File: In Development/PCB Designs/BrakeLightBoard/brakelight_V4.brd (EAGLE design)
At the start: 68.6 x 38.1 mm, 21 parts, among them Q2 30N06L

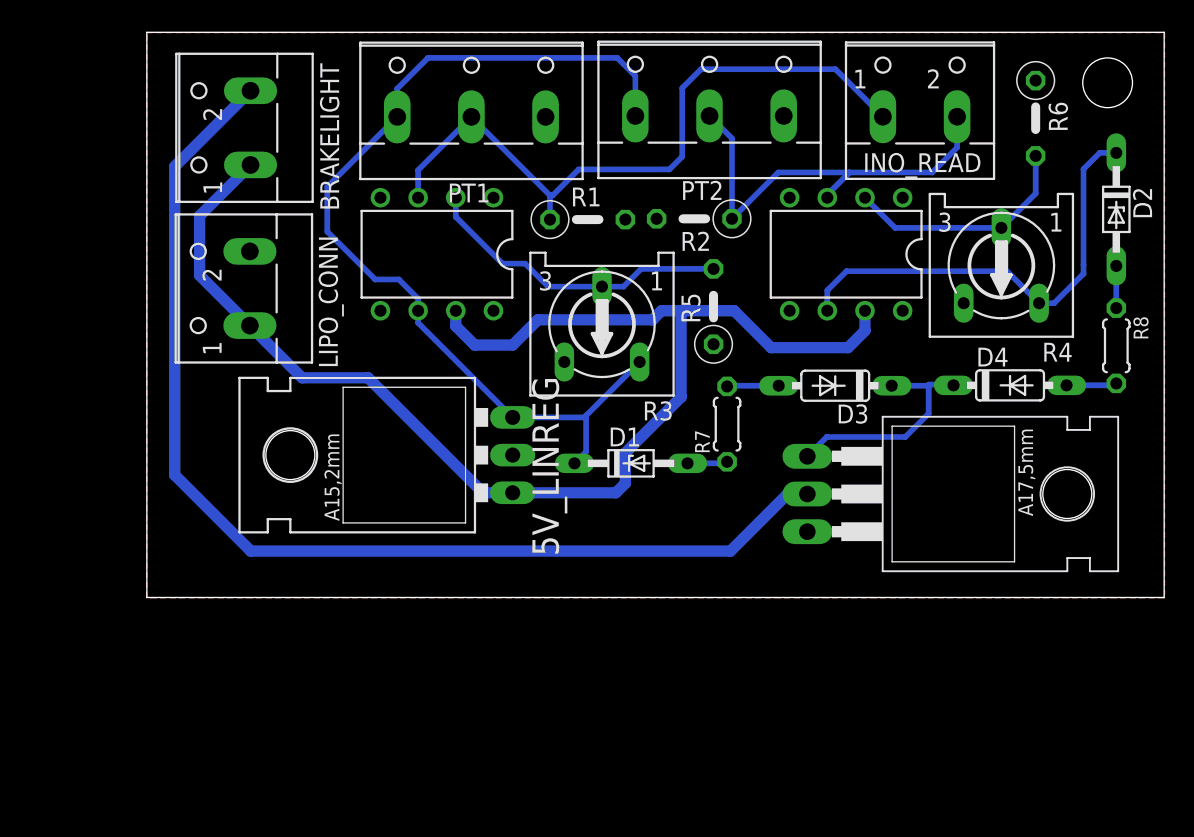
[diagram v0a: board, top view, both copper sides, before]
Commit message: Created new brakelight board using TLC2252
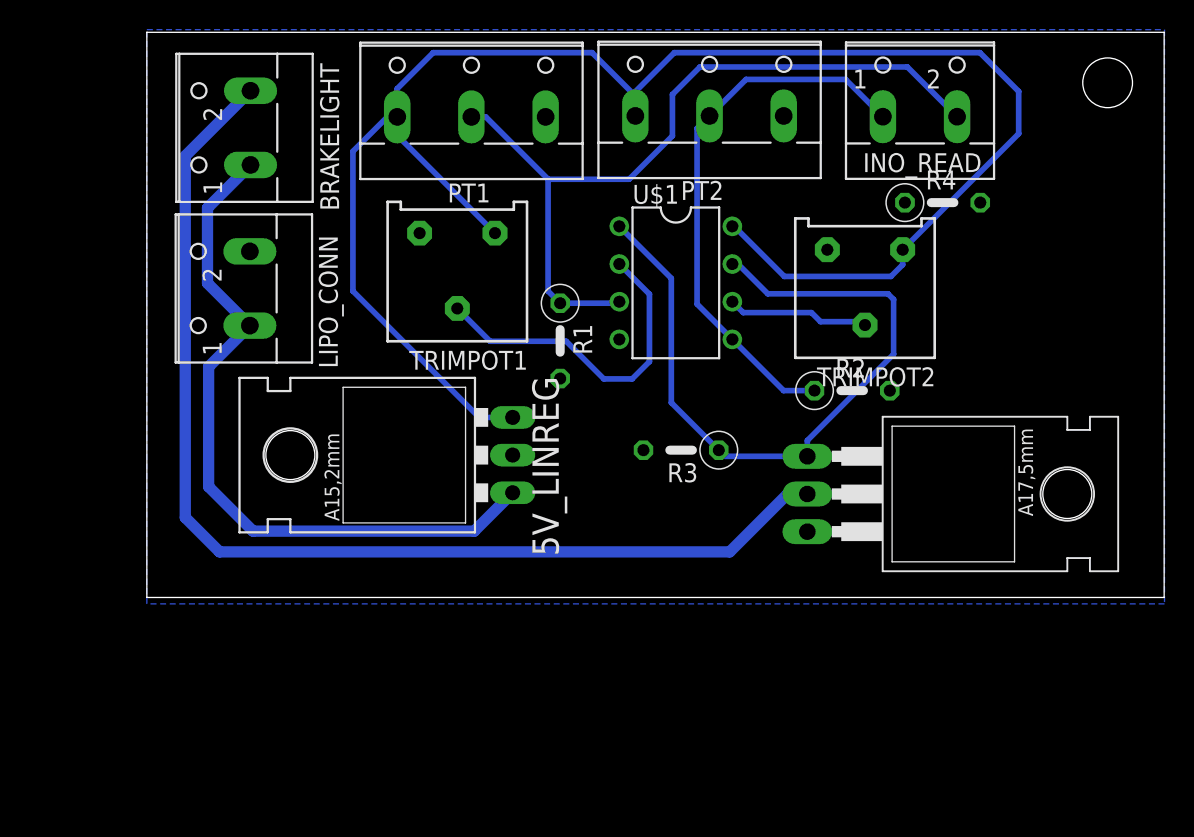
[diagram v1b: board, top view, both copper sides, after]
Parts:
- removed D1, D2: 1N5231, diode:DO34Z7
- removed D3, D4: 1N4148DO35-7, diode:DO35-7
- removed R5, R6: 560, 0ohmresistor:0207/5V
- removed R7, R8: (no value), 0ohmresistor:0204/5
- removed U$2: LM741, GTOR:DIL08
- added TRIMPOT1, TRIMPOT2: (no value), bourns:3386Y
- R1, R2: value 5.1k -> (none)
- R3, R4: value 10k -> (none); device pot:RS3 -> 0ohmresistor:0207/5V
- U$1: value LM741 -> TLC2252
- moved U$1 16.2 mm to (35.7, 21.2), turned to 270 degrees
- moved R2 15.7 mm to (47.5, 13.9), turned to 0 degrees
- moved R3 10.0 mm to (36.0, 9.93)
- moved R1 8.39 mm to (27.9, 17.3), turned to 270 degrees
- moved R4 5.80 mm to (53.6, 26.6), turned to 0 degrees
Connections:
- removed net N$4: D4.A, R8.2
- removed net N$5: D1.A, R7.1
- removed net N$6: D2.A, R8.1
- removed net N$7: D3.C, D4.C, Q2.1
- removed net THRESH1: R3.S, R5.2, U$1.2
- removed net THRESH2: R4.S, R6.2, U$2.2
- new net VREF1: TRIMPOT1.2, U$1.2
- new net VREF2: TRIMPOT2.2, U$1.6
- net 5V: now also TRIMPOT1.1, TRIMPOT2.1, U$1.8; no longer D1.C, R3.A, U$1.6
- net GND: now also R4.1, R4.2, TRIMPOT1.3, TRIMPOT2.3; no longer R5.1, R6.1, U$1.1, U$1.5, U$2.1, U$2.4, U$2.5
- net N$1: now also R3.2; no longer D2.C, R4.A, U$2.6
- net N$3: now also Q2.1, R3.1, U$1.1, U$1.7; no longer D3.A, R7.2
- net PT1: now also INO_READ.2; no longer INO_READ.1
- net PT2: now also INO_READ.1, U$1.5; no longer INO_READ.2, U$2.3
- net VCC: no longer U$1.7, U$2.7
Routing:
- net 5V: track 64.0 -> 117.5 mm
- net N$3: track 3.50 -> 48.9 mm
- net VCC: track 90.1 -> 48.0 mm
- net N$1: track 30.6 -> 0.00 mm
- net VREF1: track 0.00 -> 22.8 mm
- net THRESH1: track 21.1 -> 0.00 mm
- net THRESH2: track 15.8 -> 0.00 mm
- net N$7: track 15.5 -> 0.00 mm
- net VREF2: track 0.00 -> 9.59 mm
- net PT2: track 29.1 -> 37.1 mm
- net PT1: track 46.1 -> 53.4 mm
- net N$4: track 3.41 -> 0.00 mm
- net N$6: track 2.84 -> 0.00 mm
- net N$5: track 2.71 -> 0.00 mm
- net N$2: track 74.4 -> 75.1 mm
- added copper zone on layer 16, net N$4
- removed copper zone on layer 1, net GND

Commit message: created brakelight board prototype
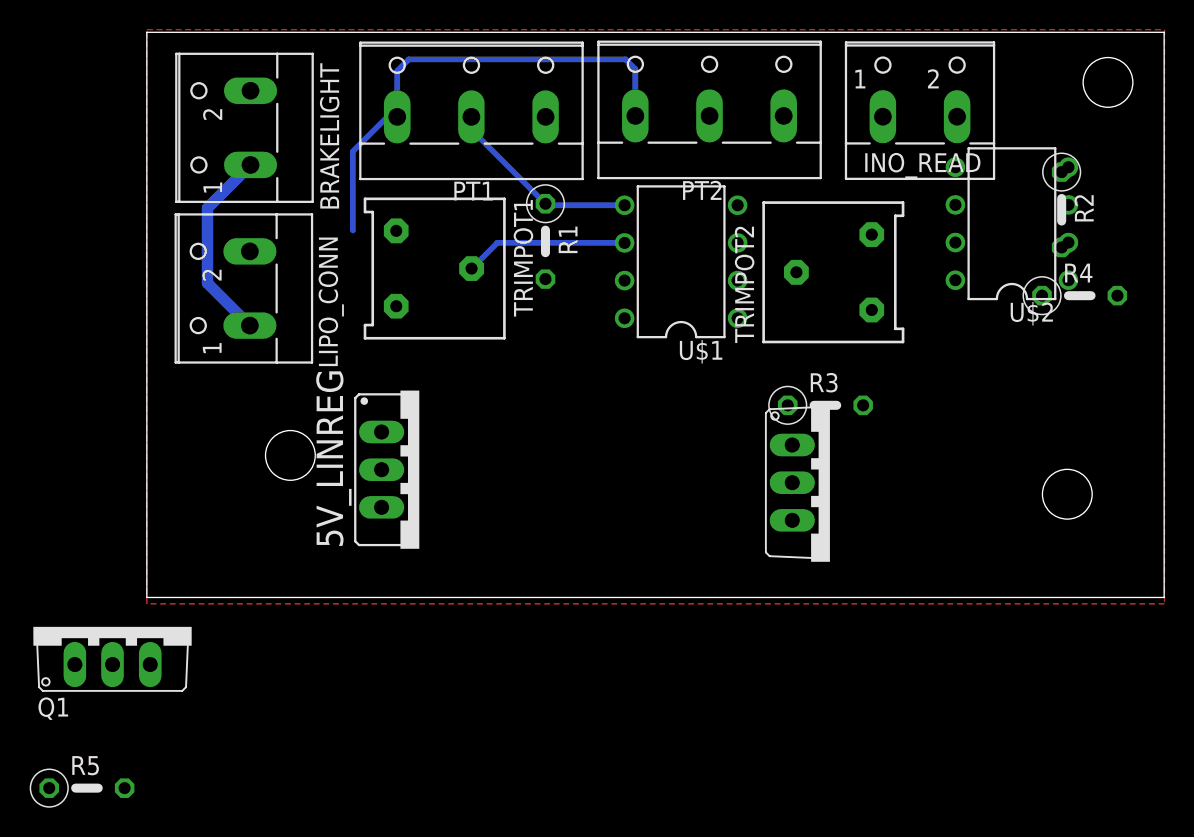
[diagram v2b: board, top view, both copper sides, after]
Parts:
- added Q1: 30N06L, FQP30N06L:TO220V
- added R5: (no value), 0ohmresistor:0207/5V
- added U$2: TLC2252, GTOR:DIL08
- added U$3, U$4, U$5: (no value), GTOR:SOLE_HOLE
- 5V_LINREG: device v-reg:78XXL -> v-reg:78XXS
- Q2: device transistor-fet:TO220 -> FQP30N06L:TO220V
- U$1: value TLC2252 -> TLV3702
- moved R2 18.7 mm to (61.7, 26.1), turned to 270 degrees
- moved R4 11.2 mm to (62.9, 20.3)
- moved R3 10.2 mm to (45.7, 13.0), turned to 0 degrees
- moved R1 6.78 mm to (26.9, 24.0)
- moved Q2 4.89 mm to (46.1, 7.74)
- moved 5V_LINREG 2.67 mm to (18.4, 8.61), turned to 270 degrees
- moved TRIMPOT2 2.32 mm to (46.3, 21.9), turned to 90 degrees
- moved TRIMPOT1 1.58 mm to (19.4, 22.2), turned to 270 degrees
- moved U$1 1.47 mm to (36.0, 22.6), turned to 90 degrees
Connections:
- new net ACTIVATE1: Q2.1, R3.1, U$1.7
- new net ACTIVATE2: Q1.1, R5.1, U$1.1
- new net N$6: INO_READ.2, U$2.1, U$2.2
- new net N$7: INO_READ.1, U$2.6, U$2.7
- net 5V: now also U$2.8
- net GND: now also Q1.2, U$2.4
- net N$2: now also Q1.3
- net N$3: now also R5.2; no longer Q2.1, R3.1, U$1.1, U$1.7
- net PT1: now also U$1.5, U$2.3; no longer INO_READ.2, U$1.3
- net PT2: now also U$1.3, U$2.5; no longer INO_READ.1, U$1.5
- net VREF1: now also U$1.6; no longer U$1.2
- net VREF2: now also U$1.2; no longer U$1.6
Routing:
- net 5V: track 117.5 -> 32.2 mm
- net N$2: track 75.1 -> 0.00 mm
- net N$3: track 48.9 -> 0.00 mm
- net PT1: track 53.4 -> 13.3 mm
- net PT2: track 37.1 -> 0.00 mm
- net VCC: track 48.0 -> 13.2 mm
- net VREF1: track 22.8 -> 11.0 mm
- net VREF2: track 9.59 -> 0.00 mm
- added copper zone on layer 1, net GND
- removed copper zone on layer 16, net N$4

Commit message: Created brd for brakelight_V4
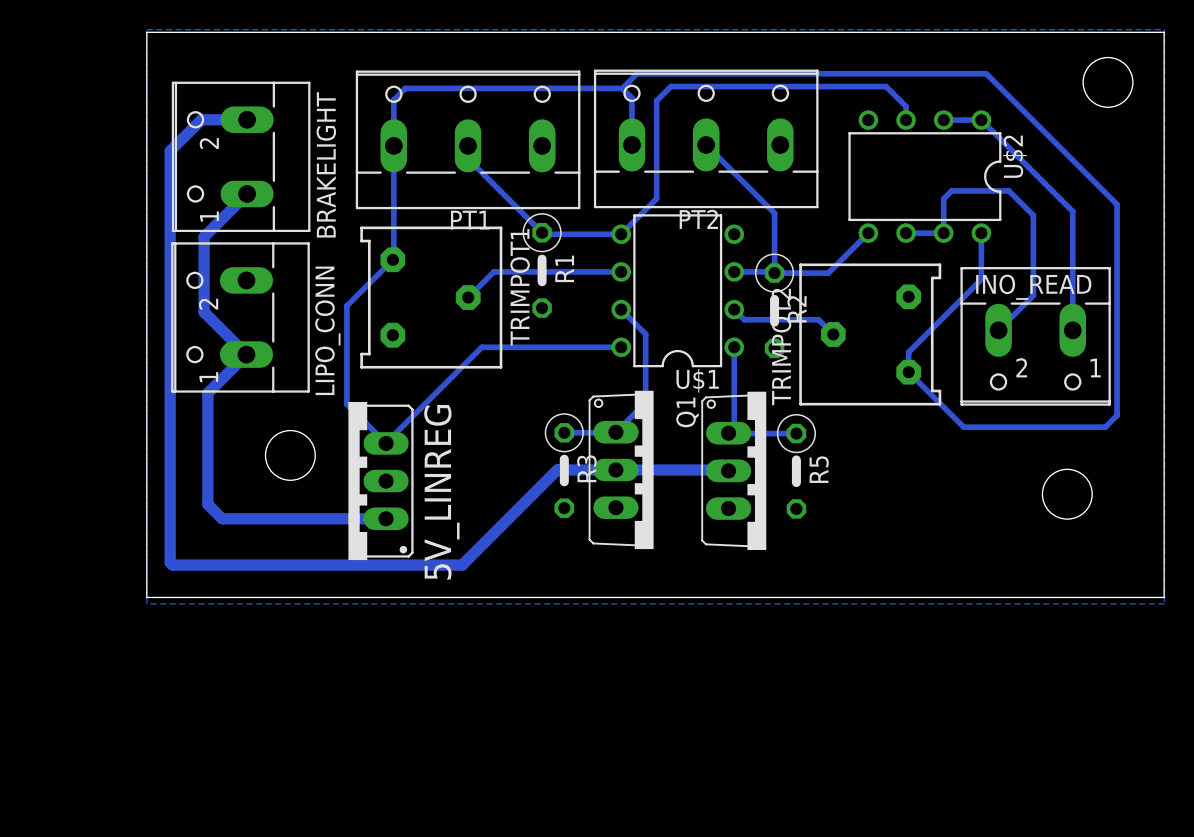
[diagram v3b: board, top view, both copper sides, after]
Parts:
- removed R4: (no value), 0ohmresistor:0207/5V
- moved R5 52.4 mm to (43.8, 8.51), turned to 270 degrees
- moved Q1 45.3 mm to (41.8, 8.53), turned to 270 degrees
- moved R2 20.5 mm to (42.3, 19.3)
- moved INO_READ 18.7 mm to (59.9, 16.7), turned to 180 degrees
- moved R3 18.1 mm to (28.1, 8.56), turned to 270 degrees
- moved Q2 11.9 mm to (34.2, 8.59)
- moved U$2 6.67 mm to (52.5, 28.4), turned to 180 degrees
- moved TRIMPOT2 4.87 mm to (48.8, 17.7)
- moved 5V_LINREG 4.84 mm to (13.6, 7.84), turned to 90 degrees
- moved BRAKELIGHT 1.97 mm to (5.49, 29.7)
- moved LIPO_CONN 1.97 mm to (5.45, 18.9)
- moved PT1 1.97 mm to (21.7, 31.7)
- moved PT2 1.97 mm to (37.7, 31.8)
- moved R1 1.97 mm to (26.6, 22.0)
- moved TRIMPOT1 1.97 mm to (19.1, 20.2)
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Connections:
- net GND: now also Q1.3; no longer Q1.2, R4.1, R4.2
- net N$2: now also Q1.2; no longer Q1.3
- net N$6: now also INO_READ.1; no longer INO_READ.2
- net N$7: now also INO_READ.2; no longer INO_READ.1
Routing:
- net 5V: track 32.2 -> 142.9 mm
- net N$2: track 0.00 -> 74.2 mm
- net PT1: track 13.3 -> 42.0 mm
- net VCC: track 13.2 -> 36.8 mm
- net PT2: track 0.00 -> 20.7 mm
- net N$7: track 0.00 -> 20.5 mm
- net N$6: track 0.00 -> 19.3 mm
- net ACTIVATE1: track 0.00 -> 13.3 mm
- net ACTIVATE2: track 0.00 -> 10.5 mm
- net VREF2: track 0.00 -> 7.37 mm
- added copper zone on layer 16, net GND
- removed copper zone on layer 1, net GND

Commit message: small revisions
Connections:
- removed net N$1: R3.2
- removed net N$3: R5.2
- net GND: now also R3.2, R5.2
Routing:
- net ACTIVATE1: track 13.3 -> 16.9 mm
- net VCC: track 36.8 -> 38.1 mm
- net N$2: track 74.2 -> 74.8 mm
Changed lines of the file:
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@@
 <drawing>
 <settings>
-<setting alwaysvectorfont="no"/>
+<setting alwaysvectorfont="yes"/>
 <setting verticaltext="up"/>
 </settings>
@@
 <contactref element="Q2" pad="3"/>
 <contactref element="Q1" pad="3"/>
+<contactref element="R5" pad="2"/>
+<contactref element="R3" pad="2"/>
 <wire x1="39.5986" y1="24.4856" x2="42.3164" y2="16.7894" width="0" layer="19" extent="1-1"/>
 <wire x1="16.5862" y1="17.6784" x2="16.1268" y2="7.845" width="0" layer="19" extent="1-1"/>
@@
 <wire x1="6.7178" y1="16.373" x2="4.1148" y2="13.77" width="0.762" layer="16"/>
 <wire x1="4.1148" y1="13.77" x2="4.1148" y2="6.2738" width="0.762" layer="16"/>
-<wire x1="4.1148" y1="6.2738" x2="5.0836" y2="5.305" width="0.762" layer="16"/>
-<wire x1="5.0836" y1="5.305" x2="16.1268" y2="5.305" width="0.762" layer="16"/>
+<wire x1="4.1148" y1="6.2738" x2="6.6838" y2="3.7048" width="0.762" layer="16"/>
+<wire x1="14.5266" y1="3.7048" x2="6.6838" y2="3.7048" width="0.762" layer="16"/>
+<wire x1="14.5266" y1="3.7048" x2="16.1268" y2="5.305" width="0.762" layer="16"/>
 </signal>
 <signal name="VREF1">
@@
 <contactref element="TRIMPOT2" pad="2"/>
 <contactref element="U$1" pad="2"/>
-<wire x1="46.2788" y1="17.7292" x2="45.2882" y2="18.7198" width="0.381" layer="16"/>
-<wire x1="45.2882" y1="18.7198" x2="40.2844" y2="18.7198" width="0.381" layer="16"/>
-<wire x1="40.2844" y1="18.7198" x2="39.5986" y2="19.4056" width="0.381" layer="16"/>
-</signal>
-<signal name="N$1">
-<contactref element="R3" pad="2"/>
+<wire x1="46.2788" y1="17.7292" x2="44.6024" y2="19.4056" width="0.381" layer="16"/>
+<wire x1="44.6024" y1="19.4056" x2="39.5986" y2="19.4056" width="0.381" layer="16"/>
 </signal>
 <signal name="N$6">
@@
 <wire x1="59.7662" y1="25.7556" x2="59.7662" y2="20.3562" width="0.381" layer="16"/>
 </signal>
-<signal name="N$3">
-<contactref element="R5" pad="2"/>
-</signal>
 <signal name="N$2">
 <contactref element="BRAKELIGHT" pad="2"/>
@@
 <wire x1="3.6778" y1="32.202" x2="1.5748" y2="30.099" width="0.762" layer="16"/>
 <wire x1="1.5748" y1="30.099" x2="1.5748" y2="2.3622" width="0.762" layer="16"/>
-<wire x1="1.7526" y1="2.1844" x2="1.5748" y2="2.3622" width="0.762" layer="16"/>
-<wire x1="1.7526" y1="2.1844" x2="21.2598" y2="2.1844" width="0.762" layer="16"/>
+<wire x1="2.4638" y1="1.4732" x2="1.5748" y2="2.3622" width="0.762" layer="16"/>
+<wire x1="2.4638" y1="1.4732" x2="20.5486" y2="1.4732" width="0.762" layer="16"/>
 <wire x1="27.67" y1="8.5946" x2="31.623" y2="8.5946" width="0.762" layer="16"/>
-<wire x1="21.2598" y1="2.1844" x2="27.67" y2="8.5946" width="0.762" layer="16"/>
+<wire x1="20.5486" y1="1.4732" x2="27.67" y2="8.5946" width="0.762" layer="16"/>
 <wire x1="31.623" y1="8.5946" x2="39.1574" y2="8.5946" width="0.762" layer="16"/>
 <wire x1="39.1574" y1="8.5946" x2="39.2176" y2="8.5344" width="0.762" layer="16"/>
@@
 <wire x1="28.1432" y1="11.0998" x2="31.5882" y2="11.0998" width="0.381" layer="16"/>
 <wire x1="31.5882" y1="11.0998" x2="31.623" y2="11.1346" width="0.381" layer="16"/>
-<wire x1="31.9786" y1="19.4056" x2="33.6296" y2="17.7546" width="0.381" layer="16"/>
-<wire x1="33.6296" y1="13.1412" x2="31.623" y2="11.1346" width="0.381" layer="16"/>
-<wire x1="33.6296" y1="17.7546" x2="33.6296" y2="13.1412" width="0.381" layer="16"/>
+<wire x1="31.9786" y1="19.4056" x2="33.9598" y2="19.4056" width="0.381" layer="16"/>
+<wire x1="35.3314" y1="18.034" x2="33.9598" y2="19.4056" width="0.381" layer="16"/>
+<wire x1="35.3314" y1="13.0142" x2="33.4518" y2="11.1346" width="0.381" layer="16"/>
+<wire x1="33.4518" y1="11.1346" x2="31.623" y2="11.1346" width="0.381" layer="16"/>
+<wire x1="35.3314" y1="18.034" x2="35.3314" y2="13.0142" width="0.381" layer="16"/>
 </signal>
 <signal name="ACTIVATE2">
